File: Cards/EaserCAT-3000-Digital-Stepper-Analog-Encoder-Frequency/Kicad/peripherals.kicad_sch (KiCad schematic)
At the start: 56 parts, among them J12 24V Field, J13 DAC, J14 In_opt1, J16 In_opt2, J18 Out_opt, J6 In1-4, J7 In5-8, J8 Output1-2, J9 Output3-4, U3 TLP292-4, U4 TLP292-4, U5 TLP292-4

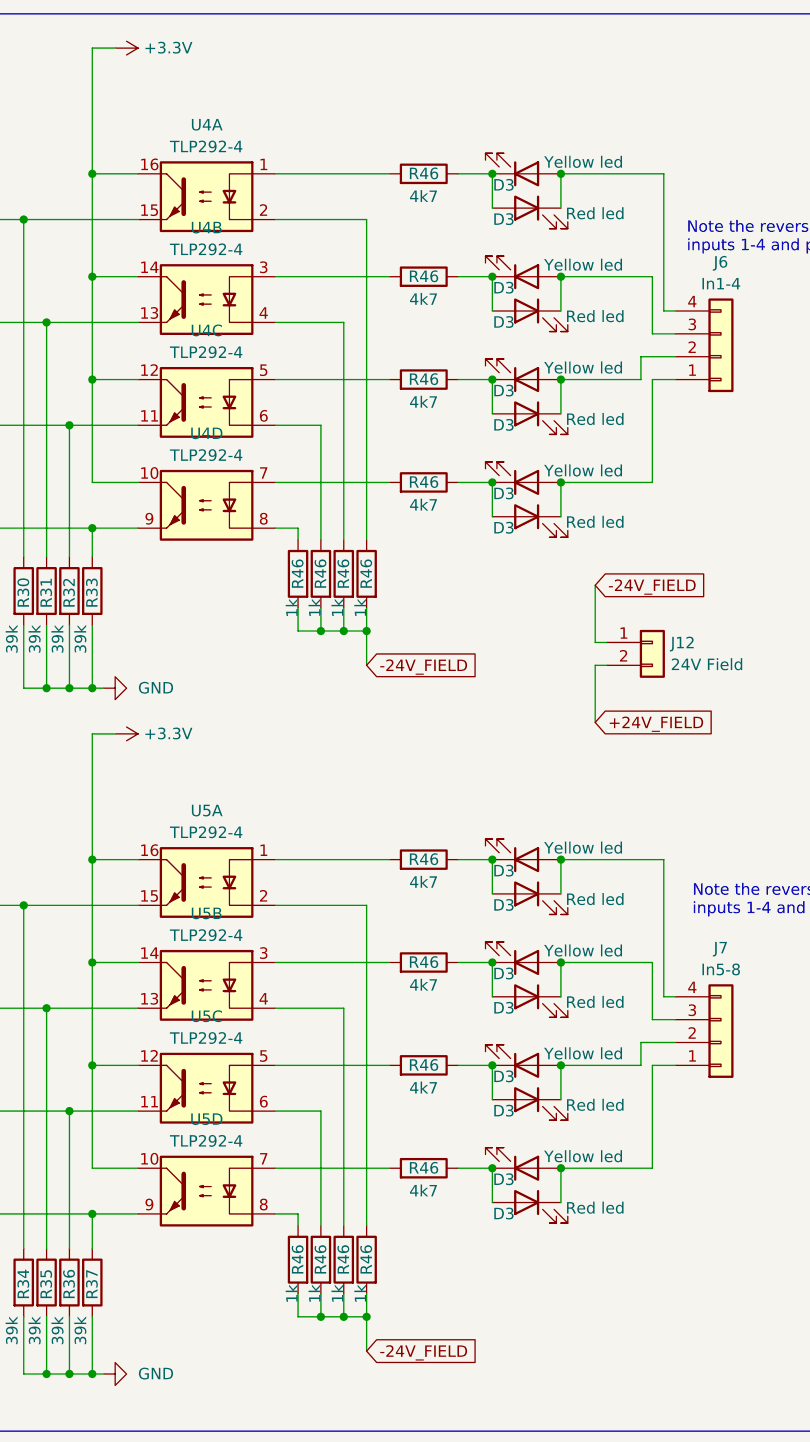
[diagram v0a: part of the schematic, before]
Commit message: Moving all to Kicad8. Housekeeping symbols,libraries,3d-models
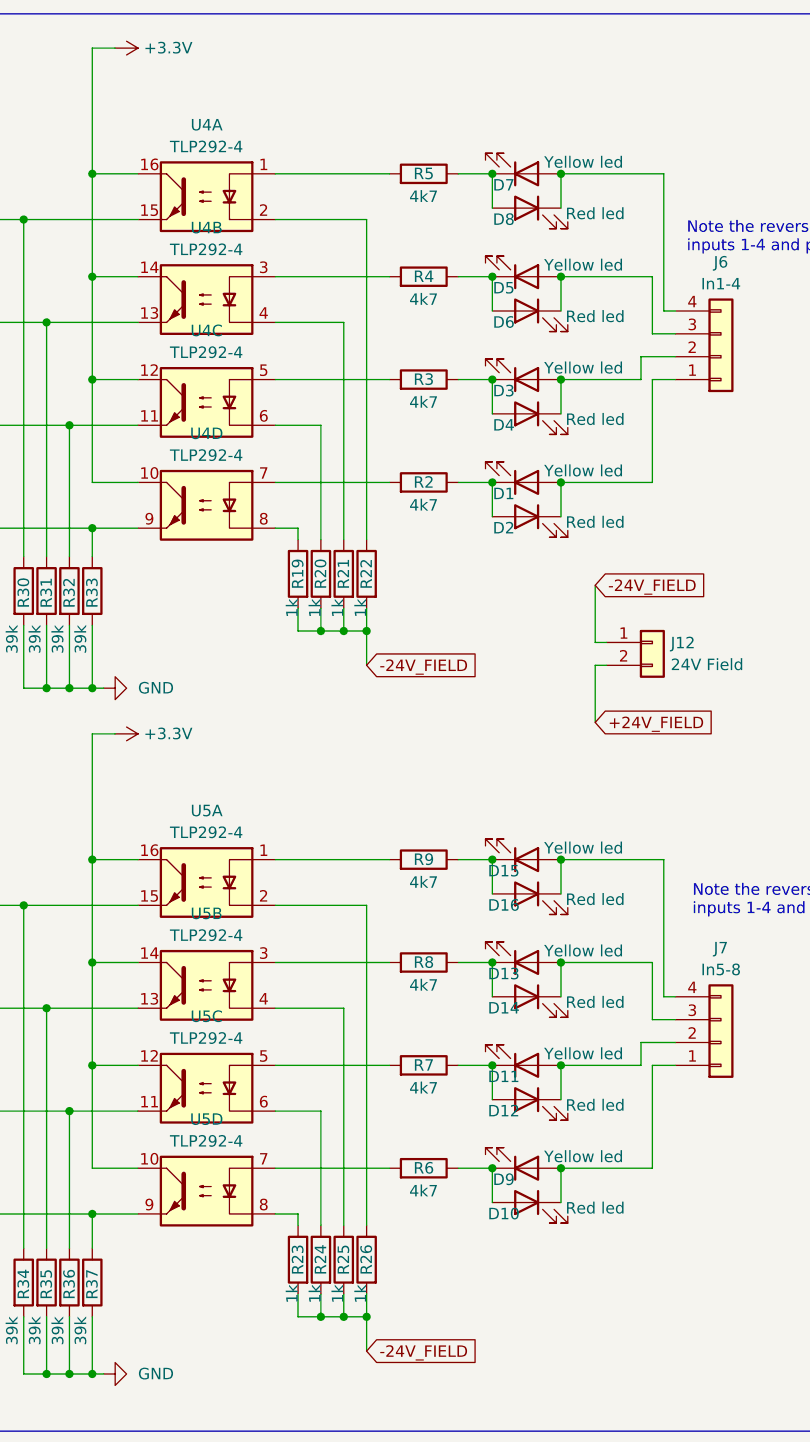
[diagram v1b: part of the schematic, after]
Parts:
- renumbered D3 to D1, D3 to D10, D3 to D11, D3 to D12, D3 to D13, D3 to D14, D3 to D15, D3 to D16, D3 to D2, D3 to D4, D3 to D5, D3 to D6, D3 to D7, D3 to D8, D3 to D9, R46 to R19, R46 to R2, R46 to R20, R46 to R21, R46 to R22, R46 to R23, R46 to R24, R46 to R25, R46 to R26, R46 to R3, R46 to R4, R46 to R5, R46 to R6, R46 to R7, R46 to R8, R46 to R9
